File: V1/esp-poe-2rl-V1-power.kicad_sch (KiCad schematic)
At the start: 32 parts

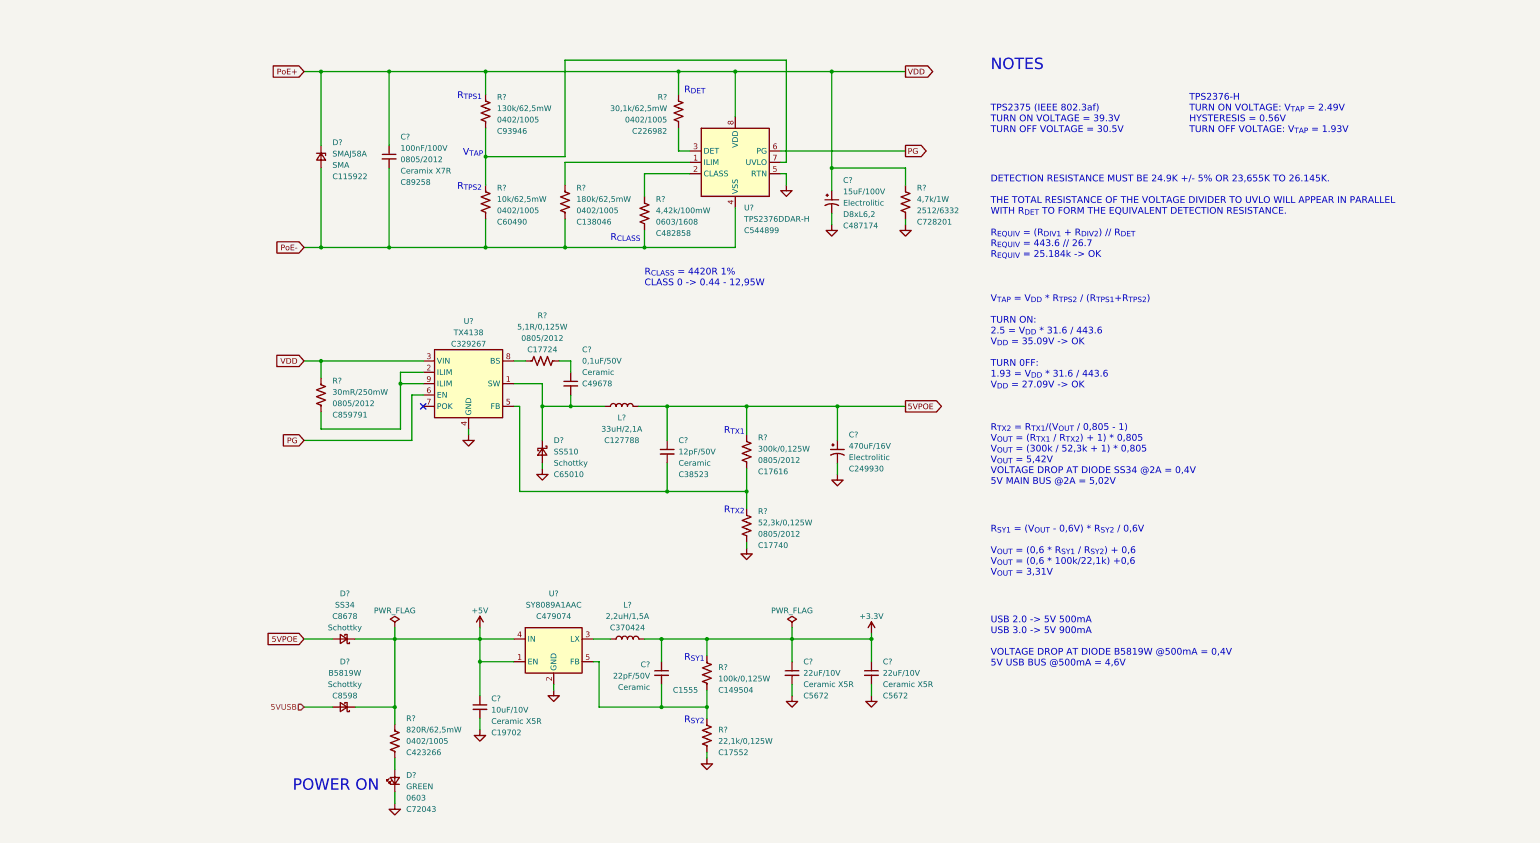
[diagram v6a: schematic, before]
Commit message: Revising components specs
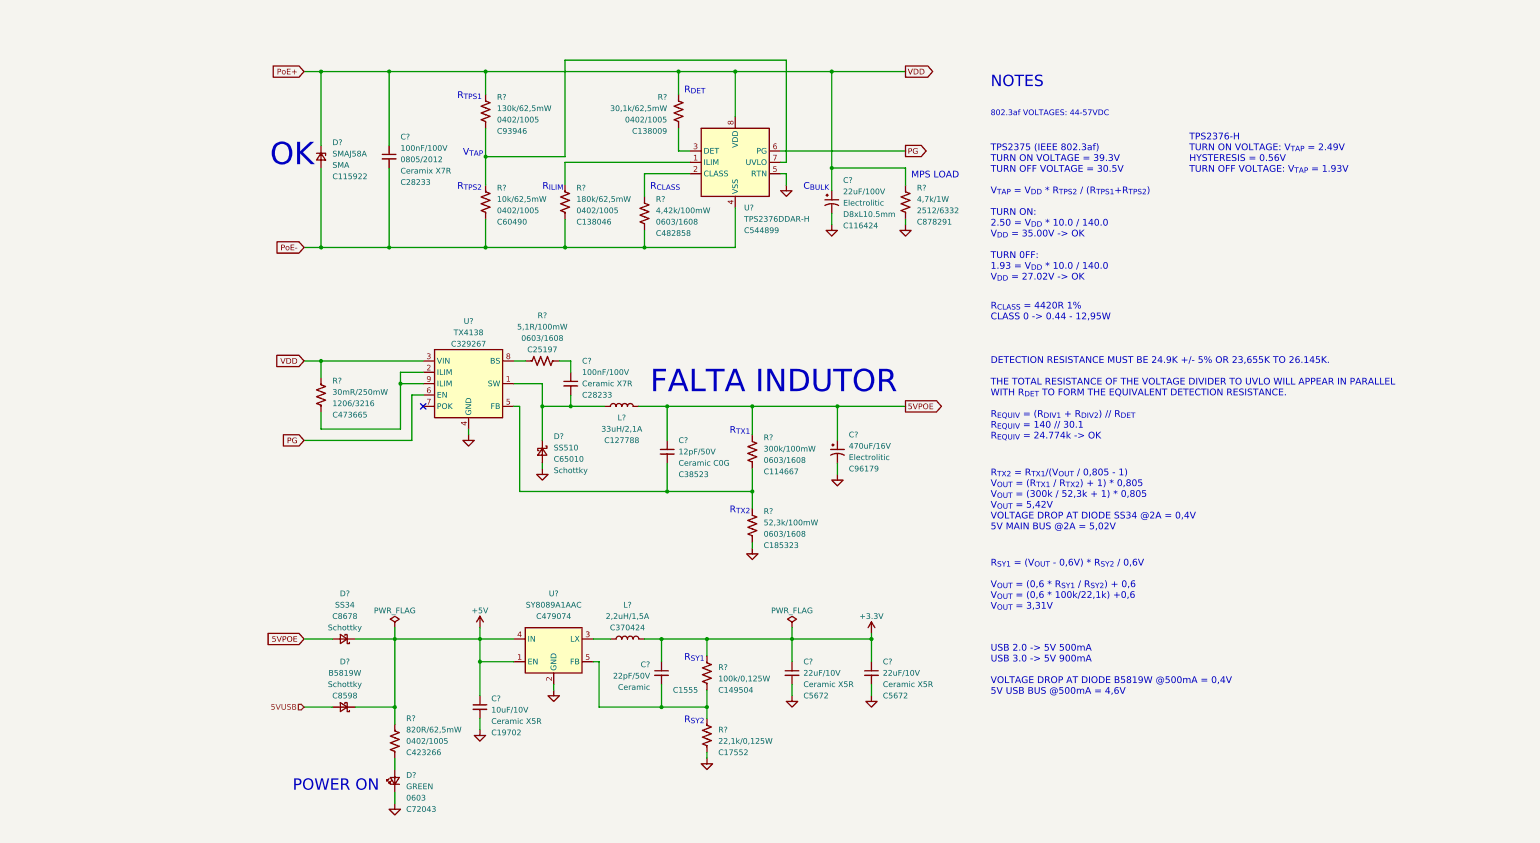
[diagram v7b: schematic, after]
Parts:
- C?: value 0,1uF/50V -> 100nF/100V; LCSC Part # C49678 -> C28233; Mfr Yageo -> Samsung; Mfr PN CC0805KRX7R9BB104 -> CL21B104KCFNNNE; Technology Ceramic -> Ceramic X7R; Vendor PN C49678 -> C28233
- C?: LCSC Part # C89258 -> C28233; Mfr FH -> Samsung; Mfr PN 0805B104K101NT -> CL21B104KCFNNNE; Vendor PN C89258 -> C28233
- C?: value 15uF/100V -> 22uF/100V; footprint Capacitor_SMD:CP_Elec_8x6.2 -> Tales:CP_Elec_8x10.5; Case D8xL6,2 -> D8xL10.5mm; LCSC Part # C487174 -> C116424; Mfr Ymin -> Semtech; Mfr PN VMMD0622A150MV -> CS2A220M-CRF10; Vendor PN C487174 -> C116424
- C?: Technology Ceramic -> Ceramic C0G
- C?: footprint Tales:CP_Elec_10x10 -> Tales:CP_Elec_8x10.5; Case 10x10 -> D8xL10.5mm; LCSC Part # C249930 -> C96179; Mfr Lelon -> Semtech; Mfr PN VZH471M1CTR-1010 -> CS1C471M-CRF10; Vendor PN C249930 -> C96179
- D?: Case SMA -> SMA/DO-214AC
- R?: value 5,1R/0,125W -> 5,1R/100mW; footprint Tales:R_0805_2012Metric -> Tales:R_0603_1608Metric; Case 0805/2012 -> 0603/1608; LCSC Part # C17724 -> C25197; Mfr PN 0805W8F510KT5E -> 0603WAF510KT5E; Vendor PN C17724 -> C25197
- R?: value 52,3k/0,125W -> 52,3k/100mW; footprint Tales:R_0805_2012Metric -> Tales:R_0603_1608Metric; Case 0805/2012 -> 0603/1608; LCSC Part # C17740 -> C185323; Mfr Uniroyal -> Yageo; Mfr PN 0805W8F5232T5E -> RC0603FR-0752K3L; Vendor PN C17740 -> C185323
- R? (x4): Mfr YAGEO -> Yageo
- R?: LCSC Part # C728201 -> C878291; Mfr YAGEO -> Yageo; Mfr PN AC2512FK-07470KL -> RC2512JK-074K7L; Vendor PN C728201 -> C878291
- R?: LCSC Part # C226982 -> C138009; Mfr YAGEO -> Yageo; Mfr PN AC0402FR-0730K1L -> RC0402FR-0730K1L; Vendor PN C226982 -> C138009
- R?: value 300k/0,125W -> 300k/100mW; footprint Tales:R_0805_2012Metric -> Tales:R_0603_1608Metric; Case 0805/2012 -> 0603/1608; LCSC Part # C17616 -> C114667; Mfr Uniroyal -> Yageo; Mfr PN 0805W8F3003T5E -> RC0603FR-07300KL; Vendor PN C17616 -> C114667
- R?: footprint Tales:R_0805_2012Metric -> Tales:R_1206_3216Metric; Case 0805/2012 -> 1206/3216; LCSC Part # C859791 -> C473665; Mfr YAGEO -> Uniroyal; Mfr PN RL0805FR-7W0R03L -> 1206W3F300MT5E; Vendor PN C859791 -> C473665
- U?: footprint Package_SO:SOIC-8-1EP_3.9x4.9mm_P1.27mm_EP2.95x4.9mm_Mask2.71x3.4mm_ThermalVias -> Tales:SOIC-8-1EP_3.9x4.9mm_P1.27mm_EP2.95x4.9mm_Mask2.71x3.4mm_ThermalVias; Technology (none) -> PD Controller
- U?: Technology (none) -> Step down DC-DC converter
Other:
- note added: "802.3af VOLTAGES: 44-57VDC"
- note added: "C_{BULK}"
- note added: "DETECTION RESISTANCE MUST BE 24.9K +/- 5% OR 23,655K TO 26.145K. THE TOTAL RESISTANCE OF THE VOLTAGE DIVIDER TO UVLO WILL APPEAR IN PARALLEL WITH R_{DET} TO FORM THE EQUIVALENT DETECTION RESISTANCE. R_{EQUIV} = (R_{DIV1} + R_{DIV2}) // R_{DET} R_{EQUIV} = 140 // 30.1 R_{EQUIV} = 24.774k -> OK"
- note added: "FALTA INDUTOR"
- note added: "MPS LOAD"
- note added: "OK"
- note added: "R_{ILIM}"
- note added: "V_{TAP} = V_{DD} * R_{TPS2} / (R_{TPS1}+R_{TPS2}) TURN ON: 2.50 = V_{DD} * 10.0 / 140.0 V_{DD} = 35.00V -> OK TURN 0FF: 1.93 = V_{DD} * 10.0 / 140.0 V_{DD} = 27.02V -> OK"
- note removed: "DETECTION RESISTANCE MUST BE 24.9K +/- 5% OR 23,655K TO 26.145K. THE TOTAL RESISTANCE OF THE VOLTAGE DIVIDER TO UVLO WILL APPEAR IN PARALLEL WITH R_{DET} TO FORM THE EQUIVALENT DETECTION RESISTANCE. R_{EQUIV} = (R_{DIV1} + R_{DIV2}) // R_{DET} R_{EQUIV} = 443.6 // 26.7 R_{EQUIV} = 25.184k -> OK"
- note removed: "V_{TAP} = V_{DD} * R_{TPS2} / (R_{TPS1}+R_{TPS2}) TURN ON: 2.5 = V_{DD} * 31.6 / 443.6 V_{DD} = 35.09V -> OK TURN 0FF: 1.93 = V_{DD} * 31.6 / 443.6 V_{DD} = 27.09V -> OK"
- moved on the sheet: R?

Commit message: Reviewing components
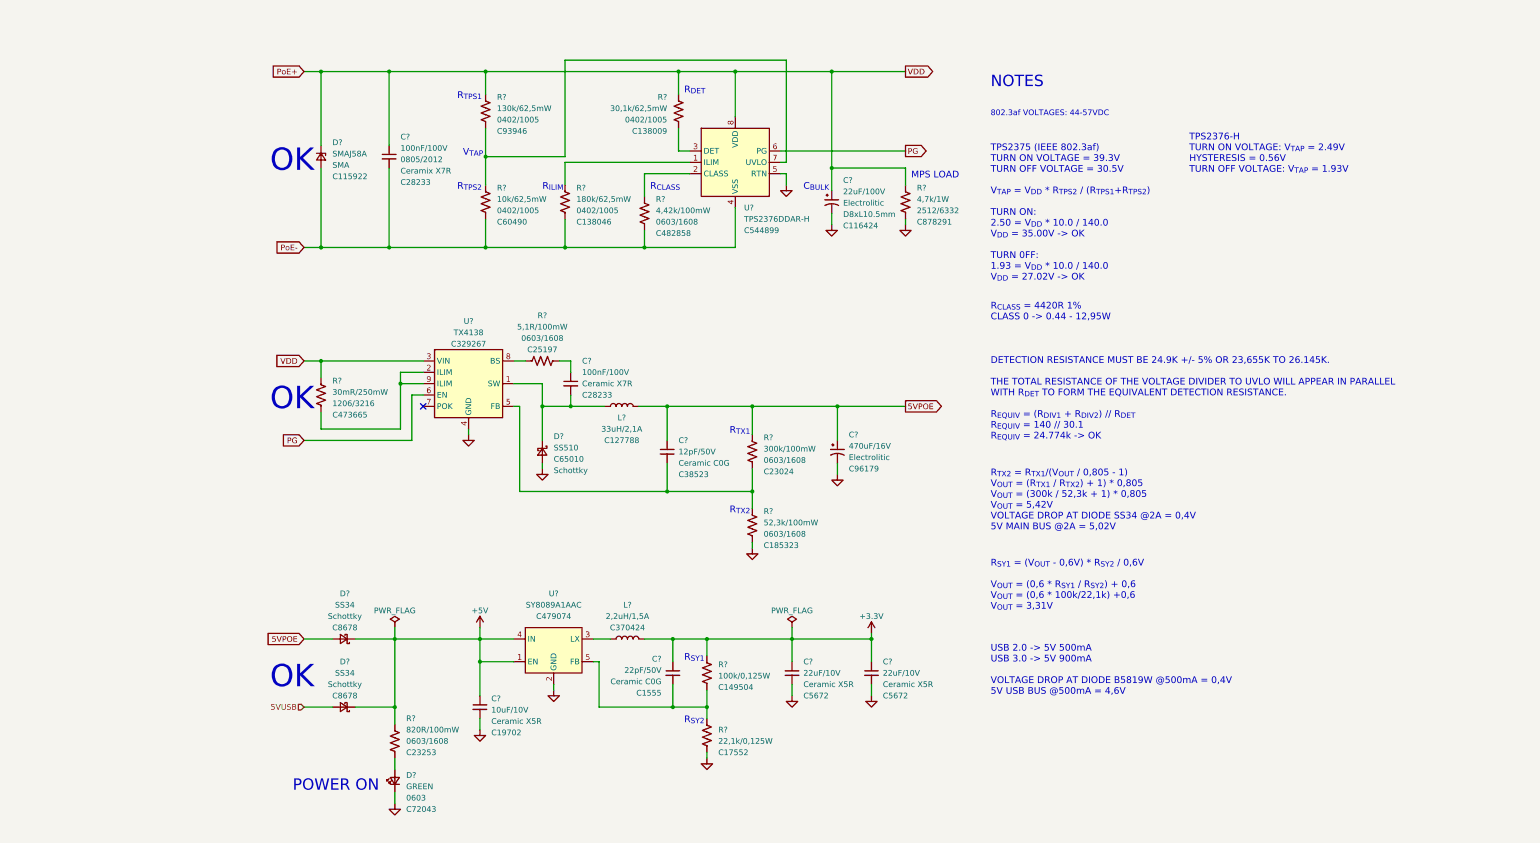
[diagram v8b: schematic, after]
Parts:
- removed D?: B5819W, Tales:D_SOD-123, symbol Device:D_Schottky_Small
- added D?: SS34, Tales:D_SMA, symbol Device:D_Schottky_Small
- C?: Technology Ceramic -> Ceramic C0G
- D?: Technology (none) -> InGaN
- R?: LCSC Part # C114667 -> C23024; Mfr Yageo -> Uniroyal; Mfr PN RC0603FR-07300KL -> 0603WAF3003T5E; Vendor PN C114667 -> C23024
- R? (x2): Technology (none) -> 1%
- R?: value 820R/62,5mW -> 820R/100mW; footprint Tales:R_0402_1005Metric -> Tales:R_0603_1608Metric; Case 0402/1005 -> 0603/1608; LCSC Part # C423266 -> C23253; Mfr PN 0402WGD8200TCE -> 0603WAF8200T5E; Technology (none) -> 1%; Vendor PN C423266 -> C23253
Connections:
- net +5V: now also D?.1 (K)
- net 5VUSB: now also D?.2 (A)
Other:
- note removed: "FALTA INDUTOR"
- moved on the sheet: C?
